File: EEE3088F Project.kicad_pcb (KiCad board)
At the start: 2 copper layers, 14 parts, among them U1 TP4056-42-ESOP8, U2 TPS62160DGK, U3 DRV8837, U4 DRV8837, U5 DRV8837, U6 DRV8837

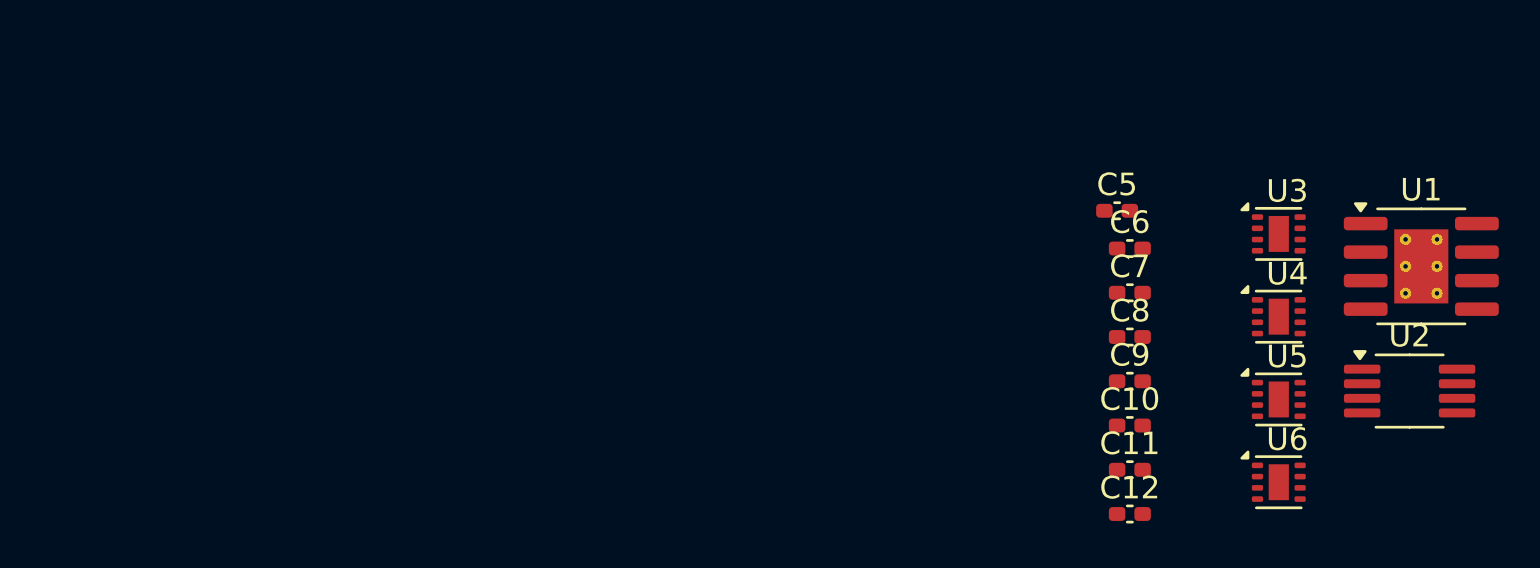
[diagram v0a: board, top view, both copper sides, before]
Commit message: changed battery charging circuit's buck converter and added mosfet circuit for charging mode selection
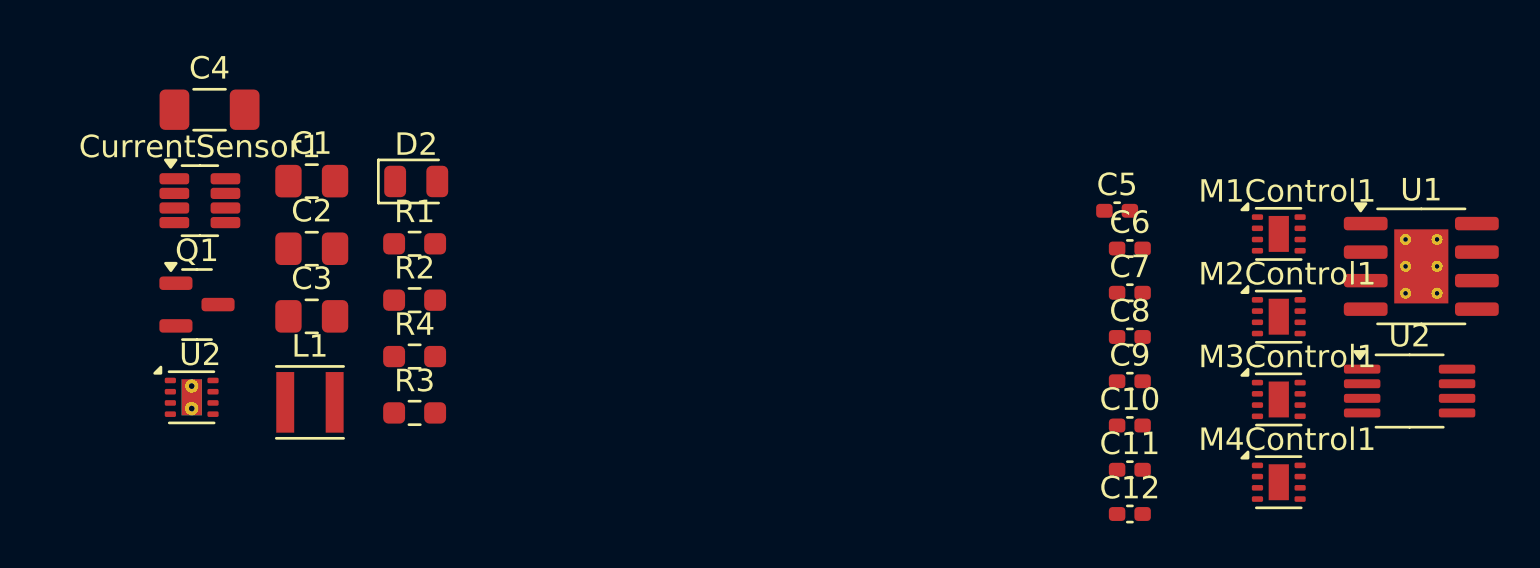
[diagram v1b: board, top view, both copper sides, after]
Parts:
- added C1: 10uF, Capacitor_SMD:C_0805_2012Metric_Pad1.18x1.45mm_HandSolder, F.Cu at (97.5, 83.2)
- added C2: 10uF, Capacitor_SMD:C_0805_2012Metric_Pad1.18x1.45mm_HandSolder, F.Cu at (97.5, 86.2)
- added C3: 10uF, Capacitor_SMD:C_0805_2012Metric_Pad1.18x1.45mm_HandSolder, F.Cu at (97.5, 89.2)
- added C4: 22uF, Capacitor_SMD:C_1206_3216Metric_Pad1.33x1.80mm_HandSolder, F.Cu at (93.0, 80.0)
- added CurrentSensor1: INA219AxDCN, Package_TO_SOT_SMD:SOT-23-8, F.Cu at (92.5, 84.0)
- added D2: RED LED, LED_SMD:LED_0805_2012Metric, F.Cu at (102.2, 83.2)
- added L1: 2.2uH, Inductor_SMD:L_Taiyo-Yuden_MD-3030, F.Cu at (97.4, 93.0)
- added Q1: AO3400A, Package_TO_SOT_SMD:SOT-23, F.Cu at (92.4, 88.7)
- added R1: 1k, Resistor_SMD:R_0603_1608Metric_Pad0.98x0.95mm_HandSolder, F.Cu at (102.1, 86.0)
- added R2: 2k7, Resistor_SMD:R_0603_1608Metric_Pad0.98x0.95mm_HandSolder, F.Cu at (102.1, 88.5)
- added R3: 5k6, Resistor_SMD:R_0603_1608Metric_Pad0.98x0.95mm_HandSolder, F.Cu at (102.1, 93.5)
- added R4: 100k, Resistor_SMD:R_0603_1608Metric_Pad0.98x0.95mm_HandSolder, F.Cu at (102.1, 91.0)
- added U2: TPS62163DSG, Package_SON:WSON-8-1EP_2x2mm_P0.5mm_EP0.9x1.6mm_ThermalVias, F.Cu at (92.2, 92.8)
- renumbered U3 to M1Control1, U4 to M2Control1, U5 to M3Control1, U6 to M4Control1
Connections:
- C10 pad 2: unconnected-(C10-Pad2) -> GND
- C11 pad 1: unconnected-(C11-Pad1) -> GND
- C12 pad 2: unconnected-(C12-Pad2) -> GND
- C5 pad 2: unconnected-(C5-Pad2) -> GND
- C6 pad 1: unconnected-(C6-Pad1) -> GND
- C7 pad 1: unconnected-(C7-Pad1) -> GND
- C8 pad 1: unconnected-(C8-Pad1) -> VBatt
- C8 pad 2: unconnected-(C8-Pad2) -> GND
- C9 pad 1: unconnected-(C9-Pad1) -> GND
- U1 pad 6: Net-(U1-~{STDBY}) -> GND

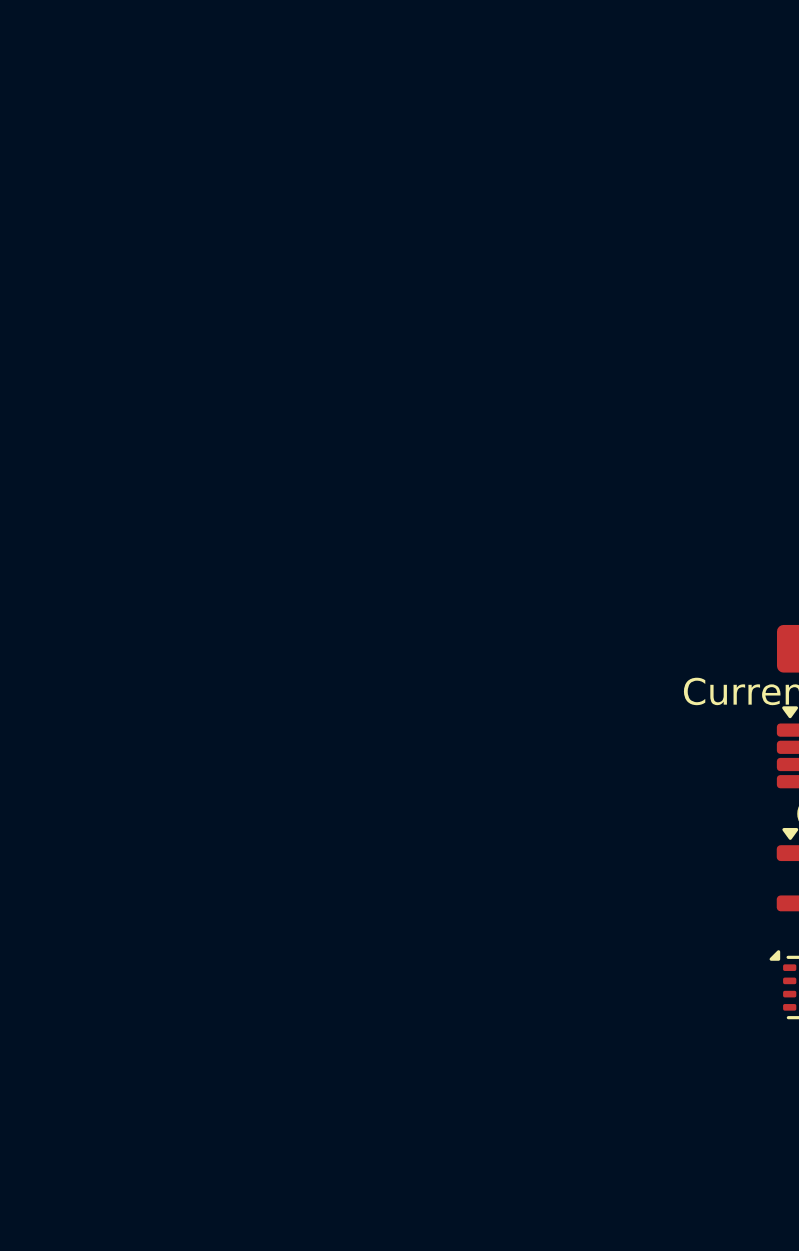
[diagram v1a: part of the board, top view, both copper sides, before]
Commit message: Finished current sensor circuit, finished battery connector circuit. Added footprints and BOM info for all.
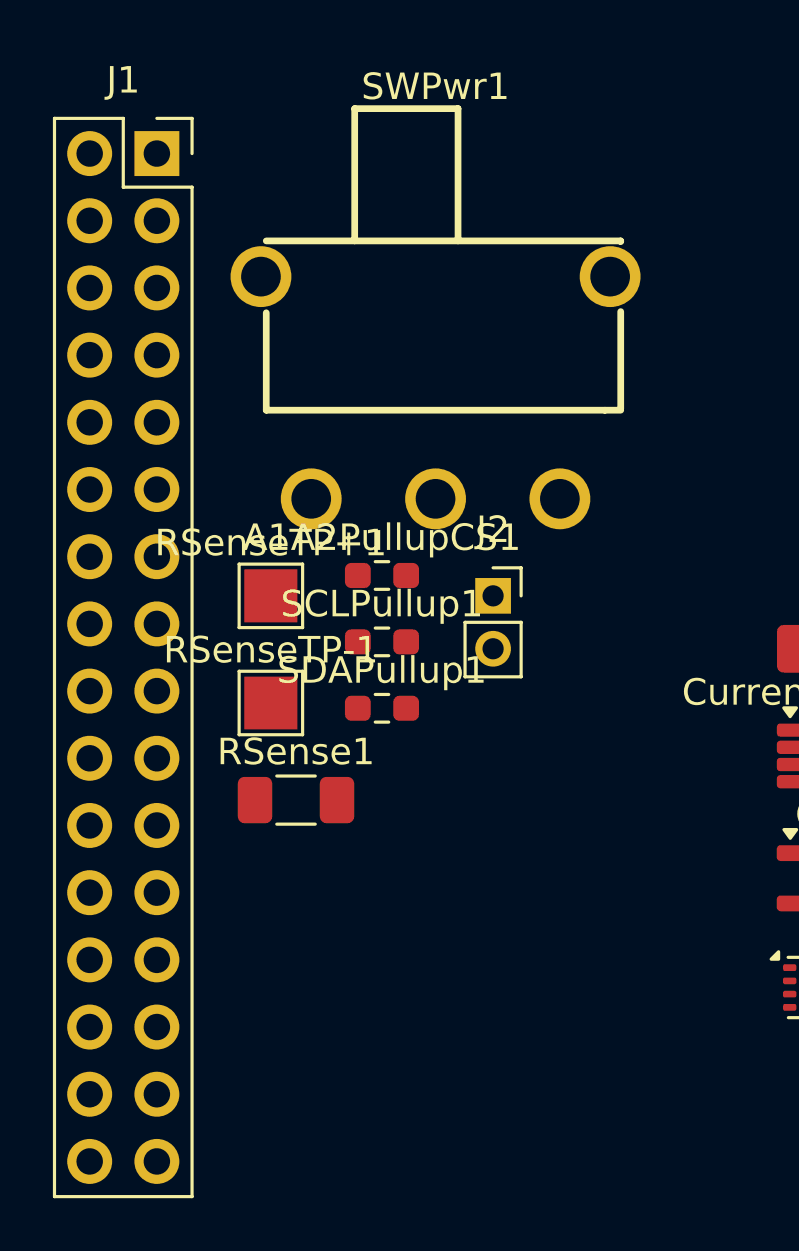
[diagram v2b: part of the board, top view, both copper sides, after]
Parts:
- added A1A2PullupCS1: 3k3, Resistor_SMD:R_0603_1608Metric_Pad0.98x0.95mm_HandSolder, F.Cu at (75.8, 77.2)
- added J1: Conn_02x16_Odd_Even, Connector_PinSocket_2.54mm:PinSocket_2x16_P2.54mm_Vertical, F.Cu at (67.3, 61.3)
- added J2: Battery IN JST, Connector_PinSocket_2.00mm:PinSocket_1x02_P2.00mm_Vertical, F.Cu at (80.0, 78.0)
- added RSense1: 0.1R, Resistor_SMD:R_1206_3216Metric_Pad1.30x1.75mm_HandSolder, F.Cu at (72.5, 85.7)
- added RSenseTP+1: TestPoint, TestPoint:TestPoint_Pad_2.0x2.0mm, F.Cu at (71.6, 78.0)
- added RSenseTP-1: TestPoint, TestPoint:TestPoint_Pad_2.0x2.0mm, F.Cu at (71.6, 82.0)
- added SCLPullup1: 3k3, Resistor_SMD:R_0603_1608Metric_Pad0.98x0.95mm_HandSolder, F.Cu at (75.8, 79.7)
- added SDAPullup1: 3k3, Resistor_SMD:R_0603_1608Metric_Pad0.98x0.95mm_HandSolder, F.Cu at (75.8, 82.2)
- added SWPwr1: SW_SPDT, Custom Footprints:SW-TH_5P-P4.70_SS-12D11-G050, F.Cu at (77.8, 70.1)
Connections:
- CurrentSensor1 pad 1: unconnected-(CurrentSensor1-IN+-Pad1) -> /RSense+
- CurrentSensor1 pad 2: unconnected-(CurrentSensor1-IN--Pad2) -> VBatt
- CurrentSensor1 pad 4: unconnected-(CurrentSensor1-VS-Pad4) -> VBatt
- CurrentSensor1 pad 5: unconnected-(CurrentSensor1-SCL-Pad5) -> /12C1_SCL
- CurrentSensor1 pad 6: unconnected-(CurrentSensor1-SDA-Pad6) -> /12C1_SDA
- M1Control1 pad 7: /PSwitch Global -> VBatt
- M2Control1 pad 7: /PSwitch Global -> VBatt
- M3Control1 pad 7: /PSwitch Global -> VBatt
- M4Control1 pad 7: /PSwitch Global -> VBatt

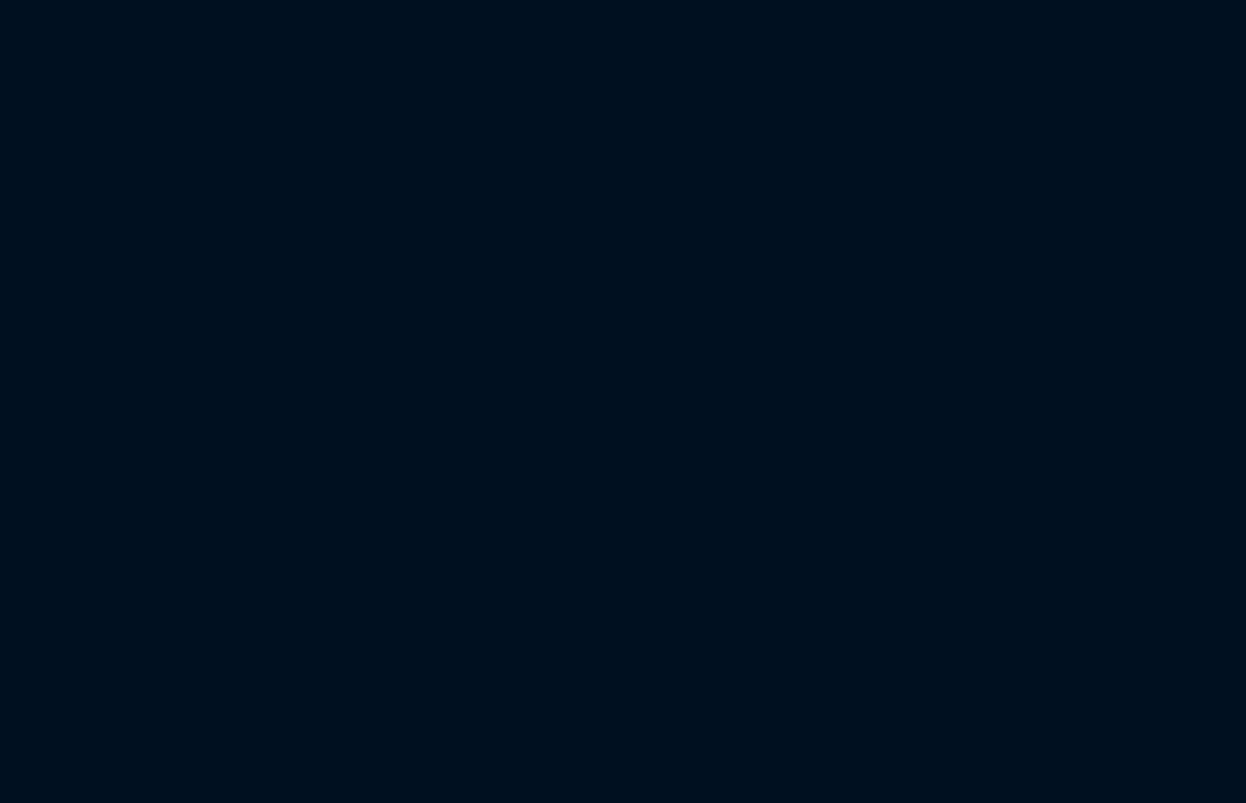
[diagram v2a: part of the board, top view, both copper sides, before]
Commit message: added 3V3 and 5V out circuitry as well as USBC
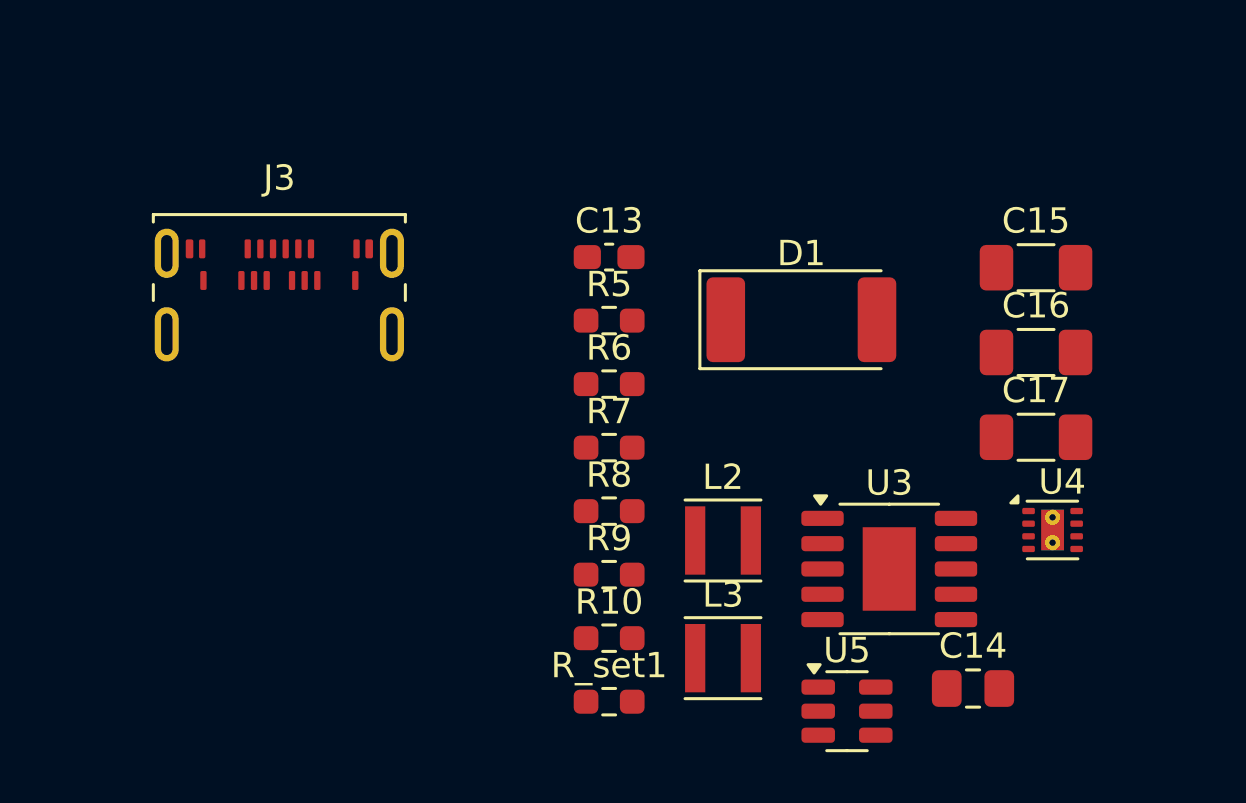
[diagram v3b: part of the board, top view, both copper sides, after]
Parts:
- added C13: 1uF, Capacitor_SMD:C_0603_1608Metric_Pad1.08x0.95mm_HandSolder, F.Cu at (96.6, 107.5)
- added C14: 10uF, Capacitor_SMD:C_0805_2012Metric_Pad1.18x1.45mm_HandSolder, F.Cu at (111.0, 124.5)
- added C15: 22uF, Capacitor_SMD:C_1206_3216Metric_Pad1.33x1.80mm_HandSolder, F.Cu at (113.5, 107.9)
- added C16: 22uF, Capacitor_SMD:C_1206_3216Metric_Pad1.33x1.80mm_HandSolder, F.Cu at (113.5, 111.2)
- added C17: 22uF, Capacitor_SMD:C_1206_3216Metric_Pad1.33x1.80mm_HandSolder, F.Cu at (113.5, 114.6)
- added D1: D_Schottky, Diode_SMD:D_2512_6332Metric_Pad1.52x3.35mm_HandSolder, F.Cu at (104.2, 109.9)
- added J3: USB_C_Receptacle_PowerOnly_24P, Connector_USB:USB_C_Receptacle_Amphenol_124019772112A, F.Cu at (83.5, 110.3)
- added L2: 2.2uH, Inductor_SMD:L_Taiyo-Yuden_MD-3030, F.Cu at (101.1, 118.7)
- added L3: 2.2uH, Inductor_SMD:L_Taiyo-Yuden_MD-3030, F.Cu at (101.1, 123.3)
- added R10: 100, Resistor_SMD:R_0603_1608Metric_Pad0.98x0.95mm_HandSolder, F.Cu at (96.6, 122.5)
- added R5: 1k, Resistor_SMD:R_0603_1608Metric_Pad0.98x0.95mm_HandSolder, F.Cu at (96.6, 110.0)
- added R6: 10k, Resistor_SMD:R_0603_1608Metric_Pad0.98x0.95mm_HandSolder, F.Cu at (96.6, 112.5)
- added R7: 100k, Resistor_SMD:R_0603_1608Metric_Pad0.98x0.95mm_HandSolder, F.Cu at (96.6, 115.0)
- added R8: 1k, Resistor_SMD:R_0603_1608Metric_Pad0.98x0.95mm_HandSolder, F.Cu at (96.6, 117.5)
- added R9: 8k2, Resistor_SMD:R_0603_1608Metric_Pad0.98x0.95mm_HandSolder, F.Cu at (96.6, 120.0)
- added R_set1: 6k8, Resistor_SMD:R_0603_1608Metric_Pad0.98x0.95mm_HandSolder, F.Cu at (96.6, 125.0)
- added U3: CH224K, Package_SO:SSOP-10-1EP_3.9x4.9mm_P1mm_EP2.1x3.3mm, F.Cu at (107.7, 119.8)
- added U4: TPS62162DSG, Package_SON:WSON-8-1EP_2x2mm_P0.5mm_EP0.9x1.6mm_ThermalVias, F.Cu at (114.1, 118.2)
- added U5: MT3608, Package_TO_SOT_SMD:SOT-23-6, F.Cu at (106.0, 125.4)
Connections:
- C3 pad 1: 9V -> VBUS
- U2 pad 2: 9V -> VBUS
- U2 pad 3: 9V -> VBUS

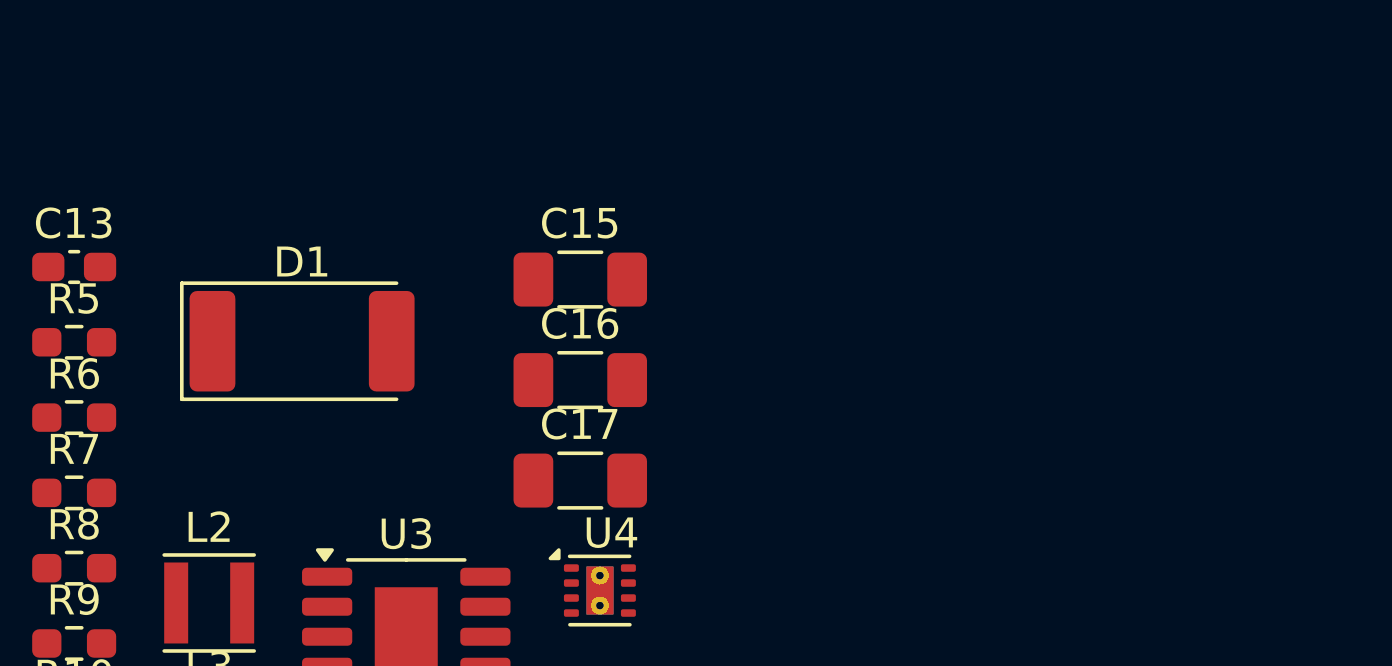
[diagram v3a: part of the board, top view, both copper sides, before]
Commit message: corrected footprints for usbc and schottky diode
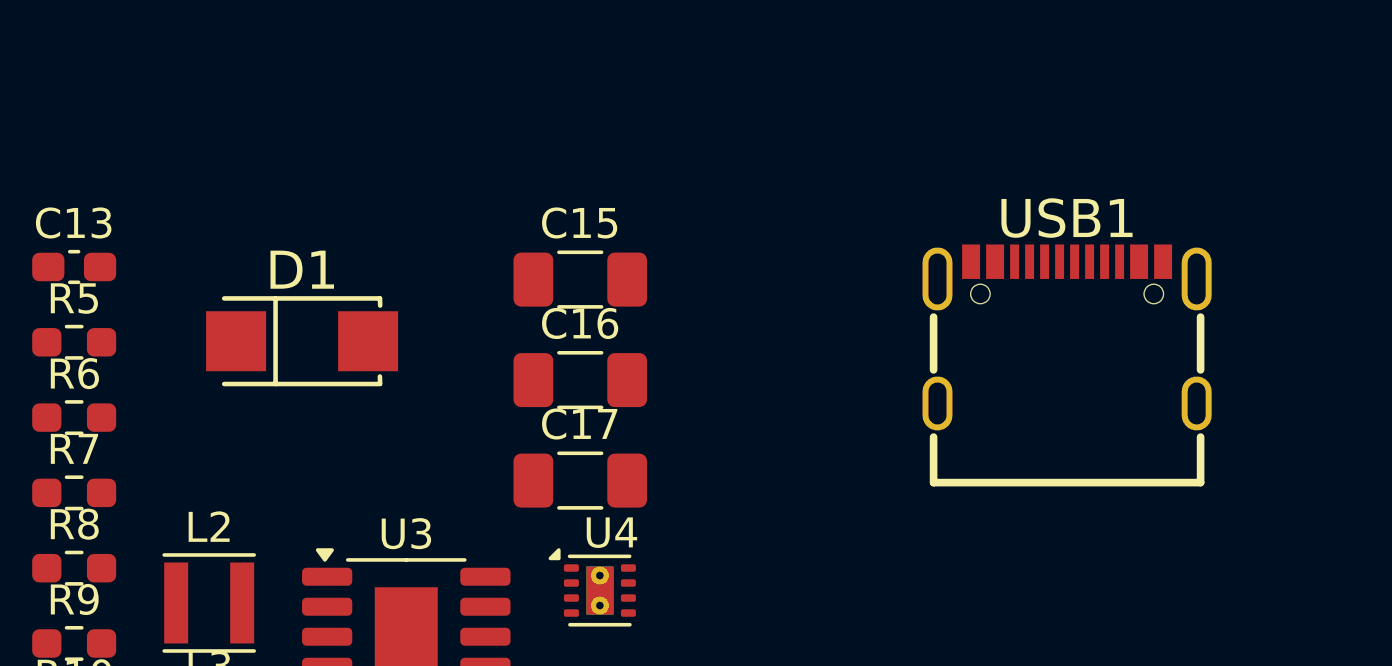
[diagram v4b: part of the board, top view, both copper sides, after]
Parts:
- added USB1: TYPE-C16PIN, TYPE-C16PIN__:USB-C-SMD_TYPE-C16PIN, F.Cu at (129.7, 109.6)
- D1: footprint Diode_SMD:D_2512_6332Metric_Pad1.52x3.35mm_HandSolder -> SMA_L4.3-W2.6-LS5.2-RD:SMA_L4.3-W2.6-LS5.2-RD
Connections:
- R5 pad 1: Net-(J3-VBUS-PadA4) -> Net-(R5-Pad1)
- U3 pad 6: Net-(J3-CC2) -> Net-(U3-CC2)
- U3 pad 7: Net-(J3-CC1) -> Net-(U3-CC1)
